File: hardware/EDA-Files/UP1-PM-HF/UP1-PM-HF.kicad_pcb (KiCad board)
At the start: 2 copper layers, 71 x 71 mm, 68 parts, among them J10 LD2420 / TOFx, J100 KNX_Conn, J101 UP1-Prog, J20 VEML7700, J30 I2C Sensor Extension, J40 Extension, J50 Binary Inputs, Q1 2N7002, SW100 Prog, U100 RP2040, U101 W25Q128JVS, Y100 12MHz

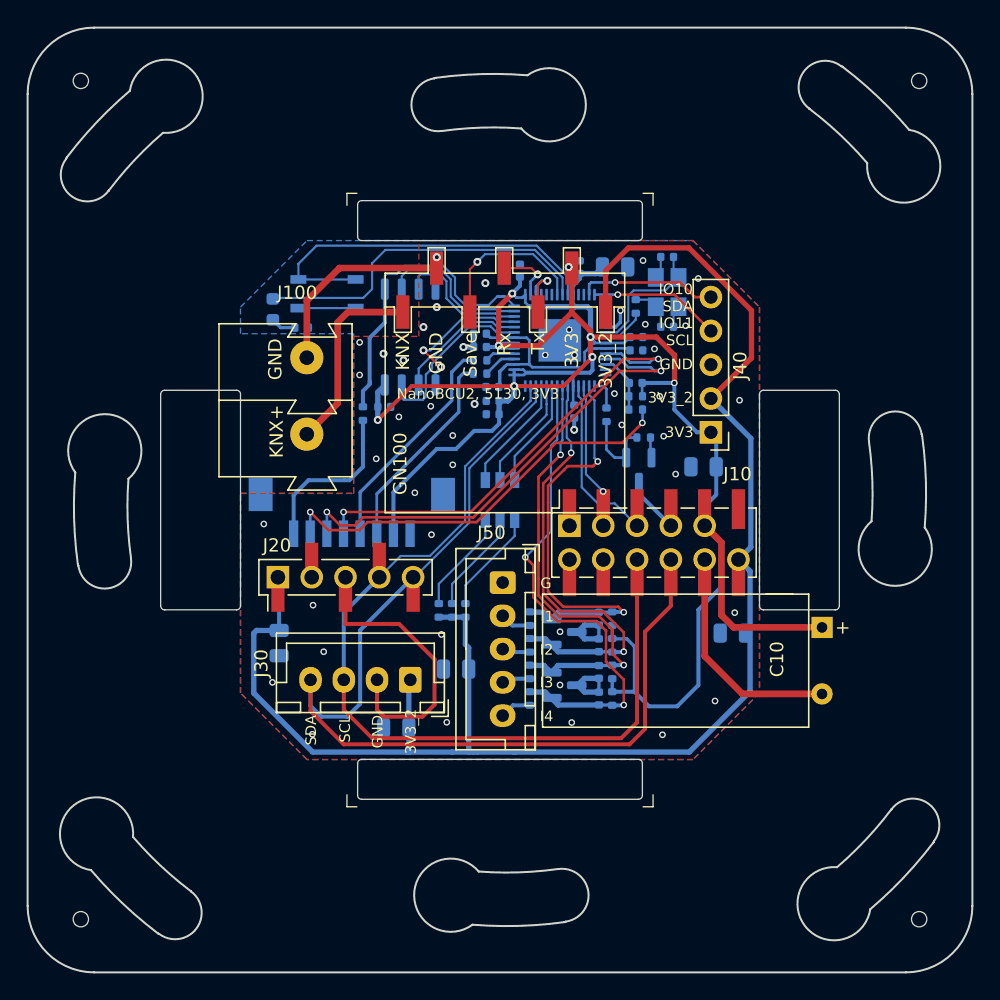
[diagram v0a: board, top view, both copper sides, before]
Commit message: UP1-PM-HF V00.20: - add reset IC
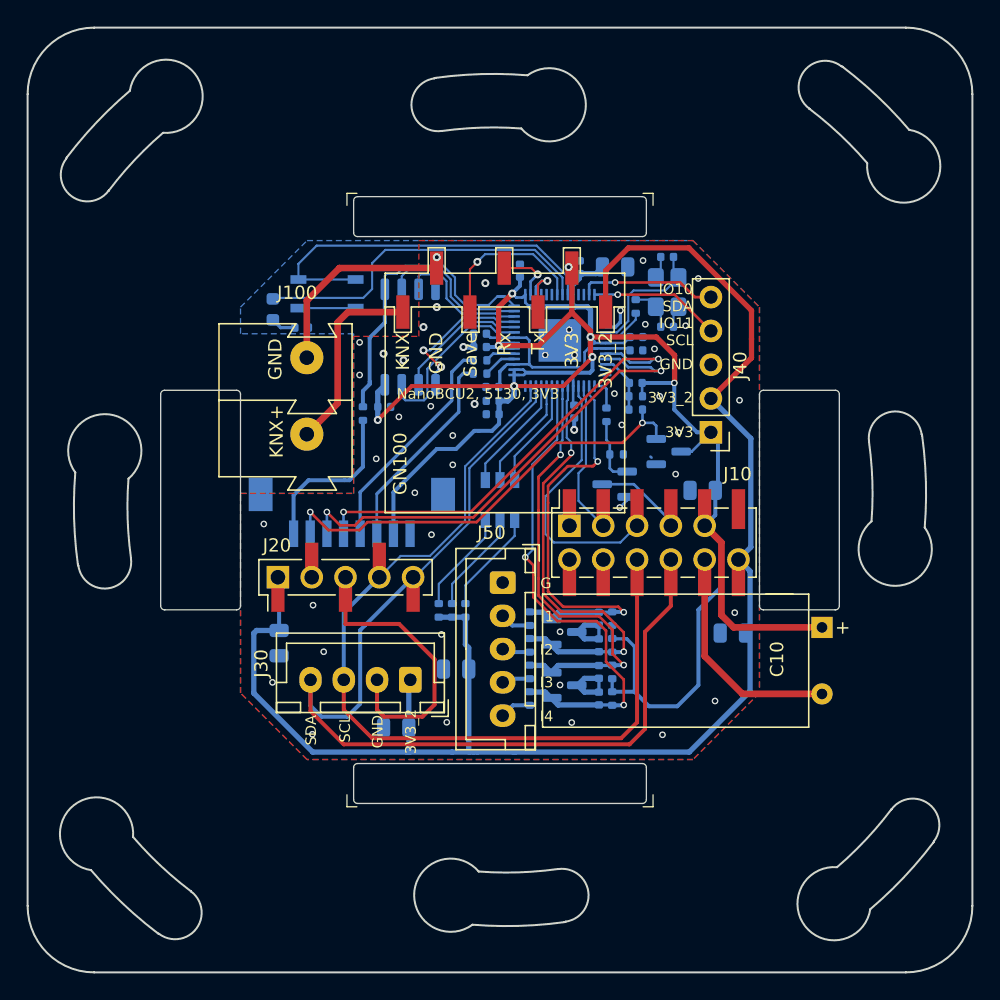
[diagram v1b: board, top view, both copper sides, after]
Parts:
- removed REF1, REF2, REF3, REF4: JLCPCB_Tooling_hole, DomsKiCADLib:JLCPCB_Tooling_hole
- added U102: MAX803R, Package_TO_SOT_SMD:SOT-23, B.Cu at (122.2, 116.9)
- U101: footprint Package_SO:SOIC-8_5.23x5.23mm_P1.27mm -> Package_SO:SOIC-8_5.3x5.3mm_P1.27mm
- moved REF6 5.66 mm to (90.9, 142.5)
- moved REF5 5.58 mm to (92.1, 100.4)
- moved R11 2.40 mm to (118.3, 117.1)
- moved Q1 2.11 mm to (118.1, 119.3), turned to 180 degrees
- moved C11 1.77 mm to (124.7, 119.8)
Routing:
- net LD2420_TX: track 13.1 -> 20.0 mm
- net LD2420_RX: track 8.66 -> 11.7 mm, vias 1 -> 0
- net +3.3V: track 161.9 -> 164.8 mm
- net Net-(Q1-D): track 4.24 -> 6.65 mm
- net RUN: track 31.5 -> 33.6 mm
- net Net-(Q1-G): track 6.06 -> 5.02 mm
- net GND: track 78.5 -> 78.1 mm, vias 46 -> 47
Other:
- outline, holes or cut-outs redrawn
- board text added: "UP1-PM-HF V00.20 by Ing-Dom, 2025"
- board text removed: "UP1-PM-HF V00.10 by Ing-Dom, 2025"

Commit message: UP1-PM-HF V00.21 * variable Flash (W25Q) * move FP to OpenKNX KiCAD Lib * increase Pad size for hand solder pins * change RP2040 reset circuit
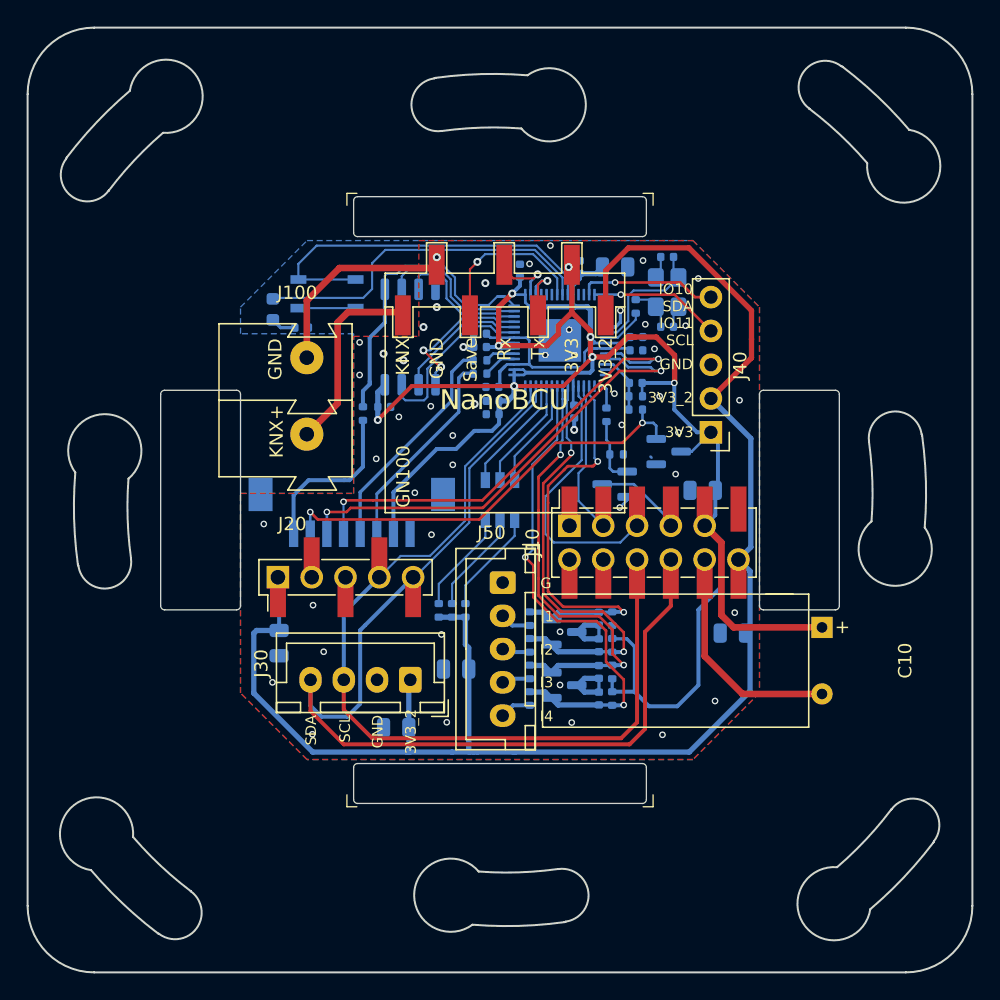
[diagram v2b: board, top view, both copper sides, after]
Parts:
- C10: footprint DomsKiCADLib:CP_Radial_D10.0mm_H20.0mm_P5.00mm_Horizontal -> OpenKNX:CP_Radial_D10.0mm_H20.0mm_P5.00mm_Horizontal
- C105: value 220pF -> 100n
- GN100: footprint OpenKNX:NanoBCU_PinHeader_SMD_low_profile -> OpenKNX:NanoBCU_PinHeader_SMD_low_profile_bigPads
- J10: footprint DomsKiCADLib:HLK_TOF_reverse_mount -> OpenKNX:HLK_TOF_reverse_mount
- J20: footprint DomsKiCADLib:VEML7700_reverse_mount -> OpenKNX:VEML7700_reverse_mount
- R105: value 2k2 -> 1k
- U101: value W25Q128JVS -> W25Q
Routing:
- net GND: track 78.1 -> 57.9 mm, vias 47 -> 49
- net +3.3V: track 164.8 -> 165.8 mm
- net SWDIO: track 36.5 -> 35.7 mm
- net KNX_Tx: track 4.45 -> 5.26 mm
- net RUN: track 33.6 -> 33.0 mm
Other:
- board text added: "UP1-PM-HF V00.21 by Ing-Dom, 2026"
- board text removed: "UP1-PM-HF V00.20 by Ing-Dom, 2025"
